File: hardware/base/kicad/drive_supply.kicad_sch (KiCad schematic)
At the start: 13 parts, among them J14 PROBE, U10 TPS1H000AQDGNRQ1, U29 TLP2361

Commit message: Harden the base board protections and unify its terminal blocks
- TVS (SMBJ33CA) on the spindle EN and DIR drains: a relay coil driven
  without a flyback diode no longer avalanches the FET.
- ESD (5 x TPD4E05U06) on every signal of the local bus header.
- A single terminal block type, KF2EDGR-3.81-4P, five times. Pinout rule:
  pole 1 withstands 24 V, pole 2 is 0 V, so the power plug damages
  nothing whichever header it lands in.
- Functional earth on pole 3 of the power terminal block, replacing the
  M3 earth lug.
- 100 k pull-down on the DAC node: the 0-10 V output stays at 0 V while
  the DAC pin is not configured (reset, bootloader).
- "24V OUT" LED on +24V_DRV and test points on the four rails.
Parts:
- removed J14: PROBE, Connector_Phoenix_MC:PhoenixContact_MC_1,5_3-G-3.81_1x03_P3.81mm_Horizontal, symbol Connector:Screw_Terminal_01x03
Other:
- note added: "PROBE: NPN sensor or dry contact between PROBE and 0 V; PROBE goes low (inverting). Terminal block shared with the emergency stop (Safety sheet)."
- note removed: "PROBE: NPN sensor or dry contact between PROBE and 0 V; PROBE goes low (inverting)."

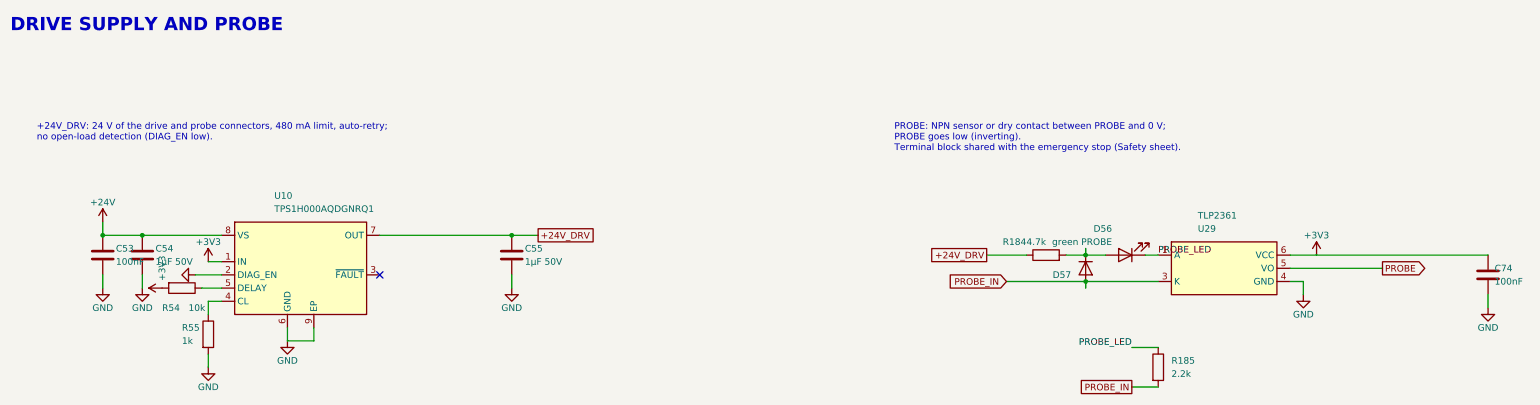
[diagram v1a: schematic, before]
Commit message: Accept a 12 V or 24 V supply on the base board (10.8 to 30 V)
- Supply nets renamed +VIN and +VIN_OUT (silkscreen VIN OUT).
- UVLO 200 k over 47 k // 100 k: start 8.47 V (9.48 V worst case),
  stop 7.79 V; fuse 3.5 A (12H1350C).
- 0-10 V: OPA2990 rail-to-rail op amp supplied by +VIN, SS8550 current
  limit across the 120 ohm; 10 V into 10 k from 10.9 V of supply.
- E-stop and probe inputs: 2 x 4.7 k in parallel, shunts 1 k and 4.7 k.
- Buck simulated from 7.8 to 30 V with the smallest slope compensation
  the datasheet allows: 79 deg, 11.6 dB minimum.
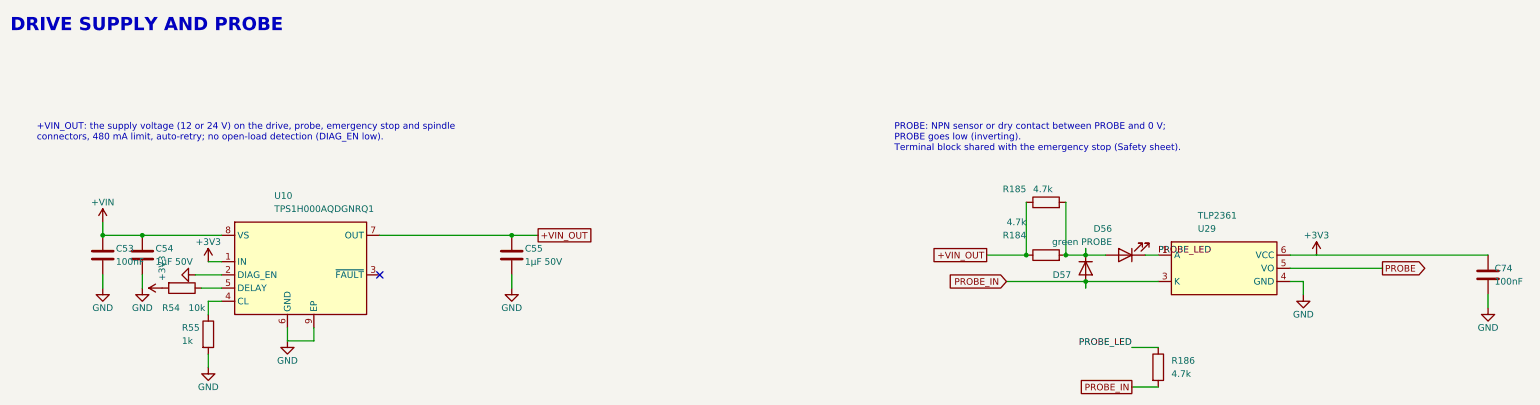
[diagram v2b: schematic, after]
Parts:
- added R186: 4.7k, Resistor_SMD:R_0402_1005Metric, symbol Device:R
- R185: value 2.2k -> 4.7k; footprint Resistor_SMD:R_0402_1005Metric -> Resistor_SMD:R_1206_3216Metric; LCSC C25879 -> C17936
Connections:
- net PROBE_IN: now also R186.2; no longer R185.2
- net PROBE_LED: now also R186.1; no longer R185.1
- net at D56.2 (A), D57.1 (K), R184.2: now also R185.2
- net +24V renamed +VIN
- net +24V_DRV renamed +VIN_OUT
- net +VIN_OUT: now also R185.1
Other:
- note added: "+VIN_OUT: the supply voltage (12 or 24 V) on the drive, probe, emergency stop and spindle connectors, 480 mA limit, auto-retry; no open-load detection (DIAG_EN low)."
- note removed: "+24V_DRV: 24 V of the drive and probe connectors, 480 mA limit, auto-retry; no open-load detection (DIAG_EN low)."
- title: 24 V of the drive ports; probe input -> VIN OUT of the drive ports; probe input
- moved on the sheet: R185
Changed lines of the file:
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@@
 	(paper "A3")
 	(title_block
-		(title "24 V of the drive ports; probe input")
+		(title "VIN OUT of the drive ports; probe input")
 		(date "2026-10-18")
 		(rev "A")
